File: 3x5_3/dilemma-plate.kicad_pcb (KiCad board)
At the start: 2 copper layers, 134 x 95.1 mm, 20 parts, among them SW101 NA_SW_Push, SW102 NA_SW_Push, SW103 NA_SW_Push, SW104 NA_SW_Push, SW106 NA_SW_Push, SW108 NA_SW_Push, SW112 NA_SW_Push, SW114 NA_SW_Push, SW115 NA_SW_Push, SW116 NA_SW_Push, SW117 NA_SW_Push, SW118 NA_SW_Push, SW119 NA_SW_Push, SW3001 NA_SW_Push

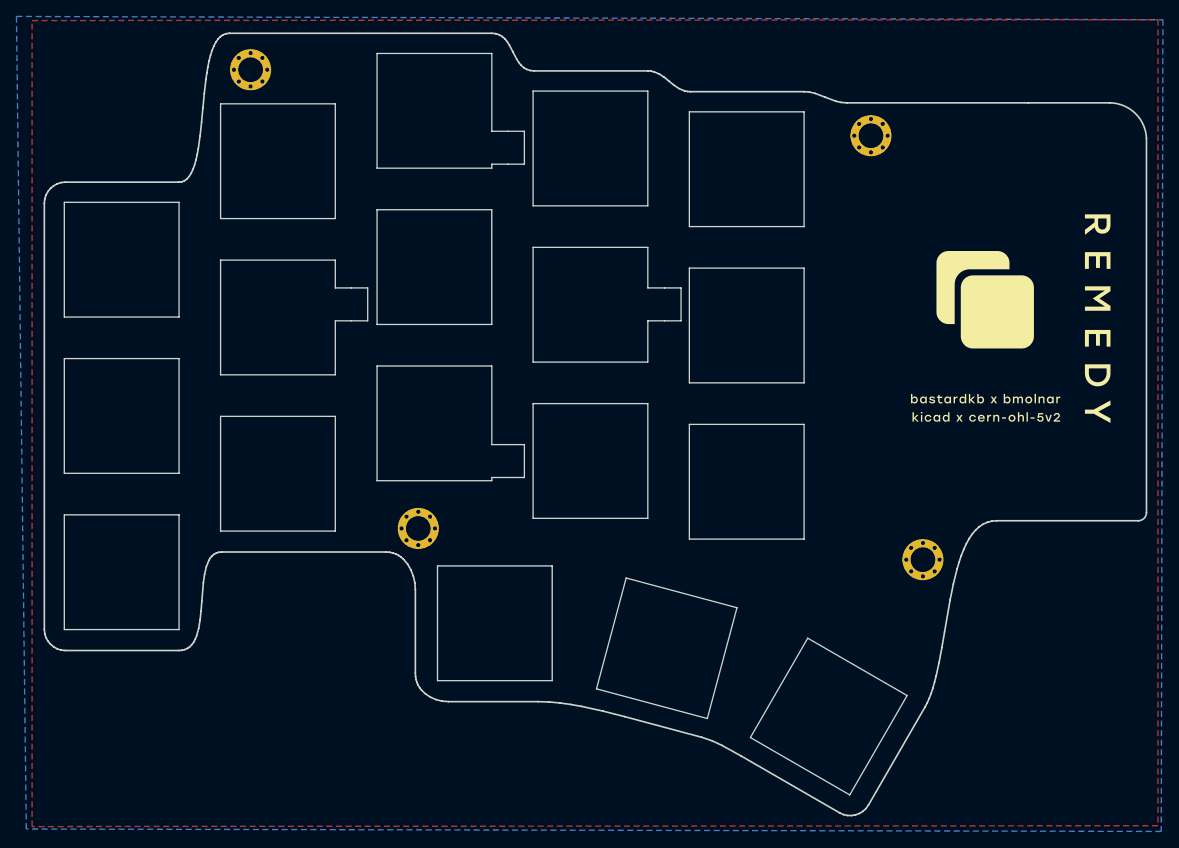
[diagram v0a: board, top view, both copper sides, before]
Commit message: antenna cutout
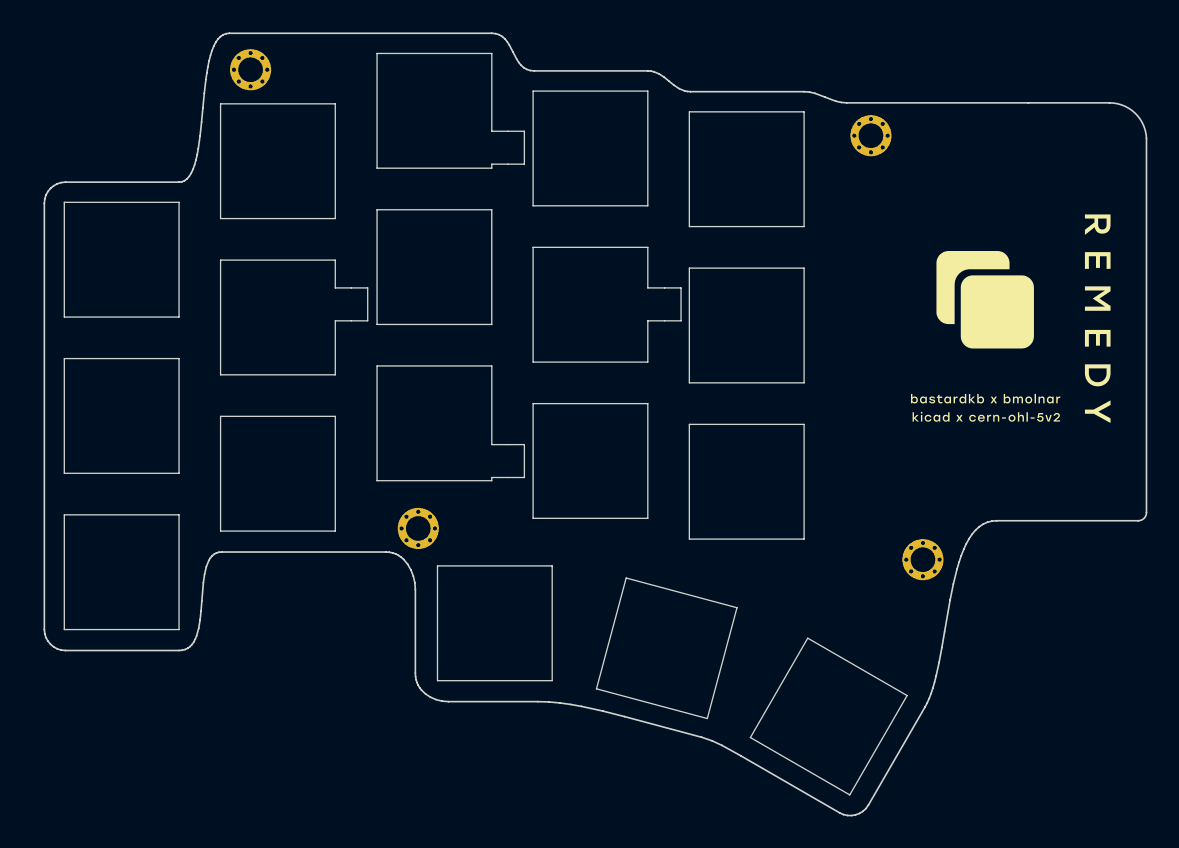
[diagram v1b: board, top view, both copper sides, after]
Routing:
- removed copper zone on B.Cu, net (none)
- removed copper zone on F.Cu, net GND
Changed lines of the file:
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@@
 				(font
 					(size 1.27 1.27)
+					(thickness 0.15)
 				)
 			)
@@
 				(font
 					(size 1.27 1.27)
+					(thickness 0.15)
 				)
 			)
@@
 				(font
 					(size 1.27 1.27)
+					(thickness 0.15)
 				)
 			)
@@
 				(font
 					(size 1.27 1.27)
+					(thickness 0.15)
 				)
 			)
@@
 				(font
 					(size 1.27 1.27)
+					(thickness 0.15)
 				)
 			)
@@
 				(font
 					(size 1.27 1.27)
+					(thickness 0.15)
 				)
 			)
@@
 				(font
 					(size 1.27 1.27)
+					(thickness 0.15)
 				)
 			)
@@
 				(font
 					(size 1.27 1.27)
+					(thickness 0.15)
 				)
 			)
@@
 				(font
 					(size 1.27 1.27)
+					(thickness 0.15)
 				)
 			)
@@
 				(font
 					(size 1.27 1.27)
+					(thickness 0.15)
 				)
 			)
@@
 				(font
 					(size 1.27 1.27)
+					(thickness 0.15)
 				)
 			)
@@
 				(font
 					(size 1.27 1.27)
+					(thickness 0.15)
 				)
 			)
@@
 				(font
 					(size 1.27 1.27)
+					(thickness 0.15)
 				)
 				(justify mirror)
@@
 				(font
 					(size 1.27 1.27)
+					(thickness 0.15)
 				)
 				(justify mirror)
@@
 				(font
 					(size 1.27 1.27)
+					(thickness 0.15)
 				)
 				(justify mirror)
@@
 				(font
 					(size 1.27 1.27)
+					(thickness 0.15)
 				)
 				(justify mirror)
@@
 				(font
 					(size 1.27 1.27)
+					(thickness 0.15)
 				)
 				(justify mirror)
@@
 				(font
 					(size 1.27 1.27)
+					(thickness 0.15)
 				)
 				(justify mirror)
@@
 				(font
 					(size 1.27 1.27)
+					(thickness 0.15)
 				)
 				(justify mirror)
@@
 				(font
 					(size 1.27 1.27)
+					(thickness 0.15)
 				)
 				(justify mirror)
@@
 				(font
 					(size 1.27 1.27)
+					(thickness 0.15)
 				)
 				(justify mirror)
@@
 				(font
 					(size 1.27 1.27)
+					(thickness 0.15)
 				)
 				(justify mirror)
@@
 				(font
 					(size 1.27 1.27)
+					(thickness 0.15)
 				)
 				(justify mirror)
@@
 				(font
 					(size 1.27 1.27)
+					(thickness 0.15)
 				)
 				(justify mirror)
@@
 				(font
 					(size 1.27 1.27)
+					(thickness 0.15)
 				)
 				(justify mirror)
@@
 				(font
 					(size 1.27 1.27)
+					(thickness 0.15)
 				)
 				(justify mirror)
@@
 				(font
 					(size 1.27 1.27)
+					(thickness 0.15)
 				)
 				(justify mirror)
@@
 				(font
 					(size 1.27 1.27)
+					(thickness 0.15)
 				)
 				(justify mirror)
@@
 				(font
 					(size 1.27 1.27)
+					(thickness 0.15)
 				)
 				(justify mirror)
@@
 				(font
 					(size 1.27 1.27)
+					(thickness 0.15)
 				)
 				(justify mirror)
@@
 				(font
 					(size 1.27 1.27)
+					(thickness 0.15)
 				)
 				(justify mirror)
@@
 				(font
 					(size 1.27 1.27)
+					(thickness 0.15)
 				)
 				(justify mirror)
@@
 				(font
 					(size 1.27 1.27)
+					(thickness 0.15)
 				)
 				(justify mirror)
@@
 				(font
 					(size 1.27 1.27)
+					(thickness 0.15)
 				)
 				(justify mirror)
@@
 				(font
 					(size 1.27 1.27)
+					(thickness 0.15)
 				)
 				(justify mirror)
@@
 				(font
 					(size 1.27 1.27)
+					(thickness 0.15)
 				)
 				(justify mirror)
@@
 				(font
 					(size 1.27 1.27)
+					(thickness 0.15)
 				)
 				(justify mirror)
@@
 				(font
 					(size 1.27 1.27)
+					(thickness 0.15)
 				)
 				(justify mirror)
@@
 				(font
 					(size 1.27 1.27)
+					(thickness 0.15)
 				)
 				(justify mirror)
@@
 				(font
 					(size 1.27 1.27)
+					(thickness 0.15)
 				)
 				(justify mirror)
@@
 				(font
 					(size 1.27 1.27)
+					(thickness 0.15)
 				)
 				(justify mirror)
@@
 				(font
 					(size 1.27 1.27)
+					(thickness 0.15)
 				)
 				(justify mirror)
@@
 				(font
 					(size 1.27 1.27)
+					(thickness 0.15)
 				)
 				(justify mirror)
@@
 				(font
 					(size 1.27 1.27)
+					(thickness 0.15)
 				)
 				(justify mirror)
@@
 				(font
 					(size 1.27 1.27)
+					(thickness 0.15)
 				)
 				(justify mirror)
@@
 				(font
 					(size 1.27 1.27)
+					(thickness 0.15)
 				)
 				(justify mirror)
@@
 				(font
 					(size 1.27 1.27)
+					(thickness 0.15)
 				)
 				(justify mirror)
@@
 				(font
 					(size 1.27 1.27)
+					(thickness 0.15)
 				)
 				(justify mirror)
@@
 				(font
 					(size 1.27 1.27)
+					(thickness 0.15)
 				)
 				(justify mirror)
@@
 				(font
 					(size 1.27 1.27)
+					(thickness 0.15)
 				)
 				(justify mirror)
@@
 				(font
 					(size 1.27 1.27)
+					(thickness 0.15)
 				)
 				(justify mirror)
@@
 				(font
 					(size 1.27 1.27)
+					(thickness 0.15)
 				)
 				(justify mirror)
@@
 				(font
 					(size 1.27 1.27)
+					(thickness 0.15)
 				)
 				(justify mirror)
@@
 				(font
 					(size 1.27 1.27)
+					(thickness 0.15)
 				)
 				(justify mirror)
@@
 		(layer "B.Fab")
 	)
-	(zone
-		(net 1)
-		(net_name "GND")
-		(layer "F.Cu")
-		(hatch edge 0.5)
-		(connect_pads
-			(clearance 0.15)
-		)
-		(min_thickness 0.25)
-		(filled_areas_thickness no)
-		(fill yes
-			(thermal_gap 0.5)
-			(thermal_bridge_width 0.5)
-		)
-		(polygon
-			(pts
-				(xy 247.868798 24.571819) (xy 247.868798 122.571819) (xy 110.968798 122.671819) (xy 110.968798 24.671819)
-			)
-		)
-	)
-	(zone
-		(net 0)
-		(net_name "")
-		(layer "B.Cu")
-		(hatch edge 0.5)
-		(priority 1)
-		(connect_pads
-			(clearance 0.15)
-		)
-		(min_thickness 0.25)
-		(filled_areas_thickness no)
-		(fill yes
-			(thermal_gap 0.5)
-			(thermal_bridge_width 0.5)
-			(island_removal_mode 1)
-			(island_area_min 10)
-		)
-		(polygon
-			(pts
-				(xy 109.068798 24.171819) (xy 248.468798 24.571819) (xy 248.268798 123.271819) (xy 110.268798 122.971819)
-			)
-		)
-	)
 	(group ""
